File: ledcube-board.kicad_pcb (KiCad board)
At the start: 4 copper layers, 181 parts, among them J1 Conn_01x02, J10 molex_53261-0871, J11 1140084168, J12 molex_53261-0871, J2 molex_53261-0871, J3 molex_53261-0871, J4 molex_53261-0871, J5 molex_53261-0871, J6 molex_53261-0871, J7 molex_53261-0871, J8 molex_53261-0871, J9 molex_53261-0871, Q1 Q_NMOS_GDSD, Q2 Q_NMOS_GDSD, Q3 Q_NMOS_GDSD, Q4 Q_NMOS_GDSD, Q5 Q_NMOS_GDSD, Q6 Q_NMOS_GDSD, Q7 Q_NMOS_GDSD, Q8 Q_NMOS_GDSD, U1 LM1085IS-12, U10 ESP32-DEVKITC-32D, U11 IP4220CZ6, U12 IP4220CZ6, U13 XC9572XL-VQ64, U14 SN74LVCC3245APWR, U15 SN74LVCC3245APWR, U2 STP08CP05MTR, U3 STP08CP05MTR, U4 STP08CP05MTR, U5 STP08CP05MTR, U6 STP08CP05MTR, U7 STP08CP05MTR, U8 STP08CP05MTR, U9 STP08CP05MTR, X1 ASE-40MHz, X2 ASE-25MHz

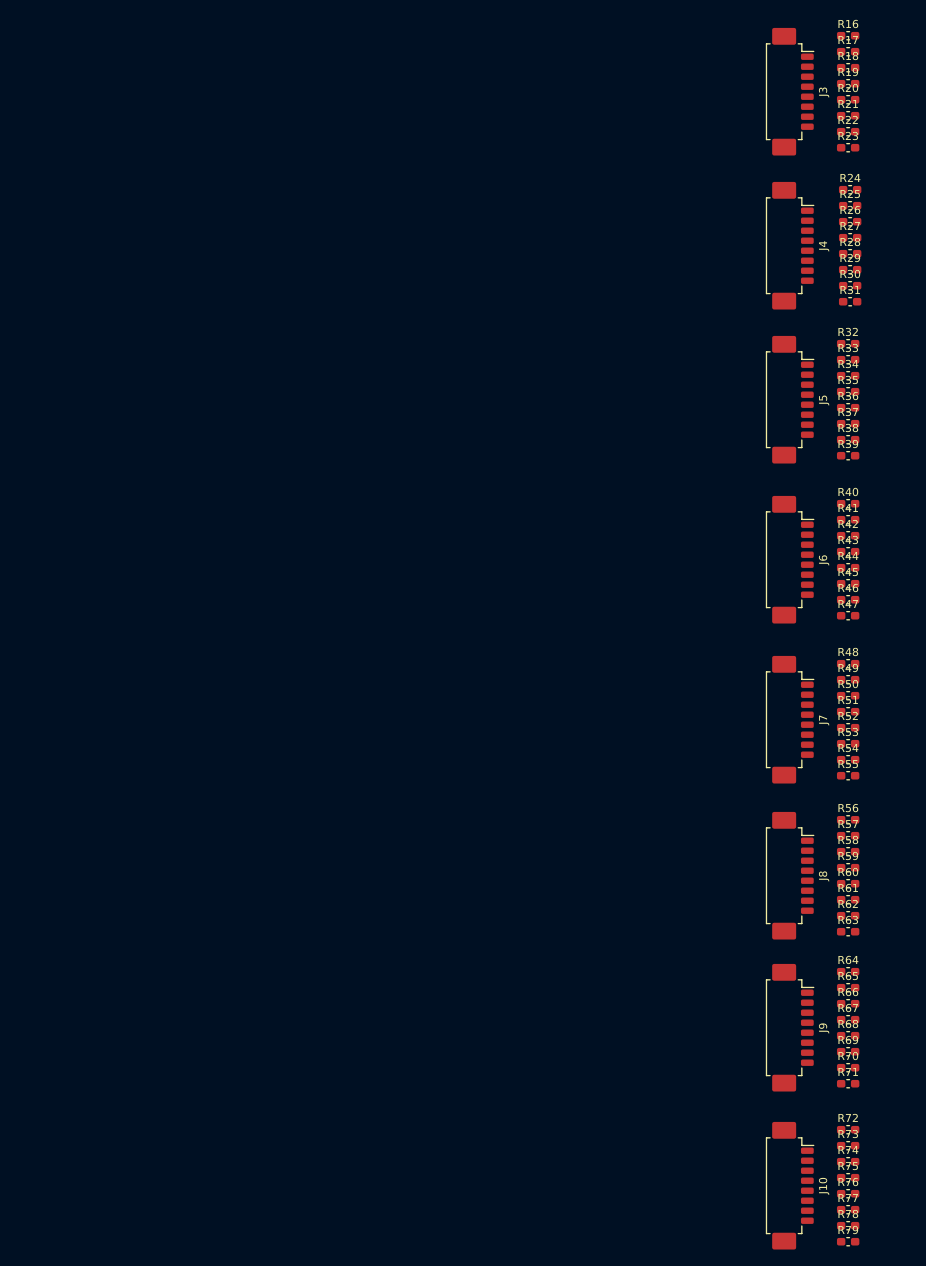
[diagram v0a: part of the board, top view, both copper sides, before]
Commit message: PCB: routing for connectors J3...J10
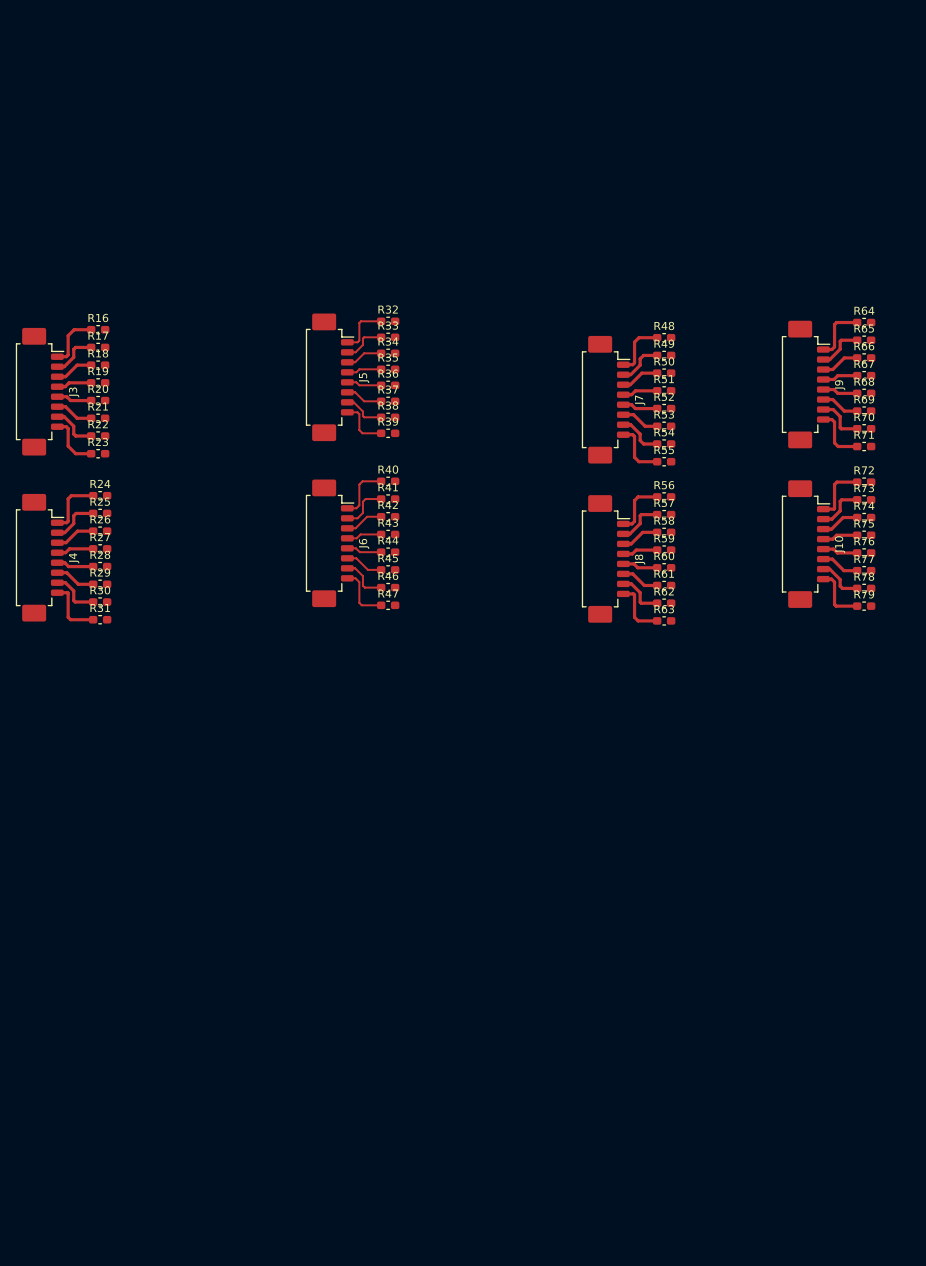
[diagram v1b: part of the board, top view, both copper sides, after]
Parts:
- moved R31 101.8 mm to (123.0, 88.5)
- moved R30 101.7 mm to (123.0, 86.3)
- moved R29 101.7 mm to (123.0, 84.1)
- moved R28 101.6 mm to (123.0, 81.9)
- moved J4 101.5 mm to (115.2, 80.8)
- moved R27 101.5 mm to (123.0, 79.6)
- moved R26 101.4 mm to (123.0, 77.4)
- moved R25 101.3 mm to (123.0, 75.2)
- moved R23 101.3 mm to (122.8, 67.8)
- moved R24 101.3 mm to (123.0, 73.0)
- moved R22 101.2 mm to (122.8, 65.5)
- moved R21 101.1 mm to (122.8, 63.3)
- moved R20 101.0 mm to (122.8, 61.1)
- moved J3 101.0 mm to (115.2, 60.0)
- moved R19 100.9 mm to (122.8, 58.9)
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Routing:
- net Net-(J4-Pad8): track 0.00 -> 7.63 mm
- net Net-(J4-Pad1): track 0.00 -> 7.51 mm
- net Net-(J10-Pad1): track 0.00 -> 7.38 mm
- net Net-(J8-Pad8): track 0.00 -> 7.26 mm
- net Net-(J10-Pad8): track 0.00 -> 7.26 mm
- net Net-(J9-Pad1): track 0.00 -> 7.26 mm
- net Net-(J6-Pad8): track 0.00 -> 7.15 mm
- net Net-(J8-Pad1): track 0.00 -> 7.15 mm
- net Net-(J7-Pad8): track 0.00 -> 7.15 mm
- net Net-(J6-Pad1): track 0.00 -> 7.15 mm
- net Net-(J7-Pad1): track 0.00 -> 7.15 mm
- net Net-(J9-Pad8): track 0.00 -> 7.15 mm
- net Net-(J3-Pad1): track 0.00 -> 7.03 mm
- net Net-(J3-Pad8): track 0.00 -> 6.91 mm
- net Net-(J5-Pad1): track 0.00 -> 6.60 mm
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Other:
- net class led_pwr added: clearance 0.3, trace_width 0.4, via_dia 1, via_drill 0.5

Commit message: Complete routing of single part of led connectors
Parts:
- moved U6 392.7 mm to (-48.2, 73.0)
- moved U7 382.1 mm to (-49.2, 95.2)
- moved C12 370.9 mm to (-47.4, 87.6), turned to 180 degrees
- moved C11 361.4 mm to (-46.4, 65.5), turned to 180 degrees
- moved C14 354.7 mm to (-14.2, 59.8), turned to 180 degrees
- moved U9 348.7 mm to (-16.0, 67.3)
- moved U8 347.6 mm to (14.0, 74.1)
- moved C13 319.5 mm to (15.8, 66.6), turned to 180 degrees
- moved C8 302.1 mm to (62.6, 57.5), turned to 180 degrees
- moved U3 283.9 mm to (60.8, 65.0)
- moved C9 282.2 mm to (70.4, 77.4), turned to 270 degrees
- moved U2 279.1 mm to (60.8, 44.2)
- moved C7 278.9 mm to (62.6, 36.7), turned to 180 degrees
- moved U4 269.1 mm to (78.0, 79.2), turned to 90 degrees
- moved U5 255.5 mm to (98.7, 79.2), turned to 90 degrees
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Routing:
- net Net-(R39-Pad2): track 0.00 -> 22.6 mm
- net Net-(R47-Pad2): track 0.00 -> 22.6 mm
- net Net-(R31-Pad2): track 0.00 -> 22.6 mm
- net Net-(R79-Pad2): track 0.00 -> 22.6 mm
- net Net-(R71-Pad2): track 0.00 -> 22.6 mm
- net Net-(R63-Pad2): track 0.00 -> 22.6 mm
- net Net-(R23-Pad2): track 0.00 -> 22.6 mm
- net Net-(R55-Pad2): track 0.00 -> 22.6 mm
- net Net-(R46-Pad2): track 0.00 -> 20.1 mm
- net Net-(R38-Pad2): track 0.00 -> 20.1 mm
- net Net-(R22-Pad2): track 0.00 -> 20.1 mm
- net Net-(R62-Pad2): track 0.00 -> 20.1 mm
- net Net-(R54-Pad2): track 0.00 -> 20.1 mm
- net Net-(R30-Pad2): track 0.00 -> 20.1 mm
- net Net-(R70-Pad2): track 0.00 -> 20.1 mm
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
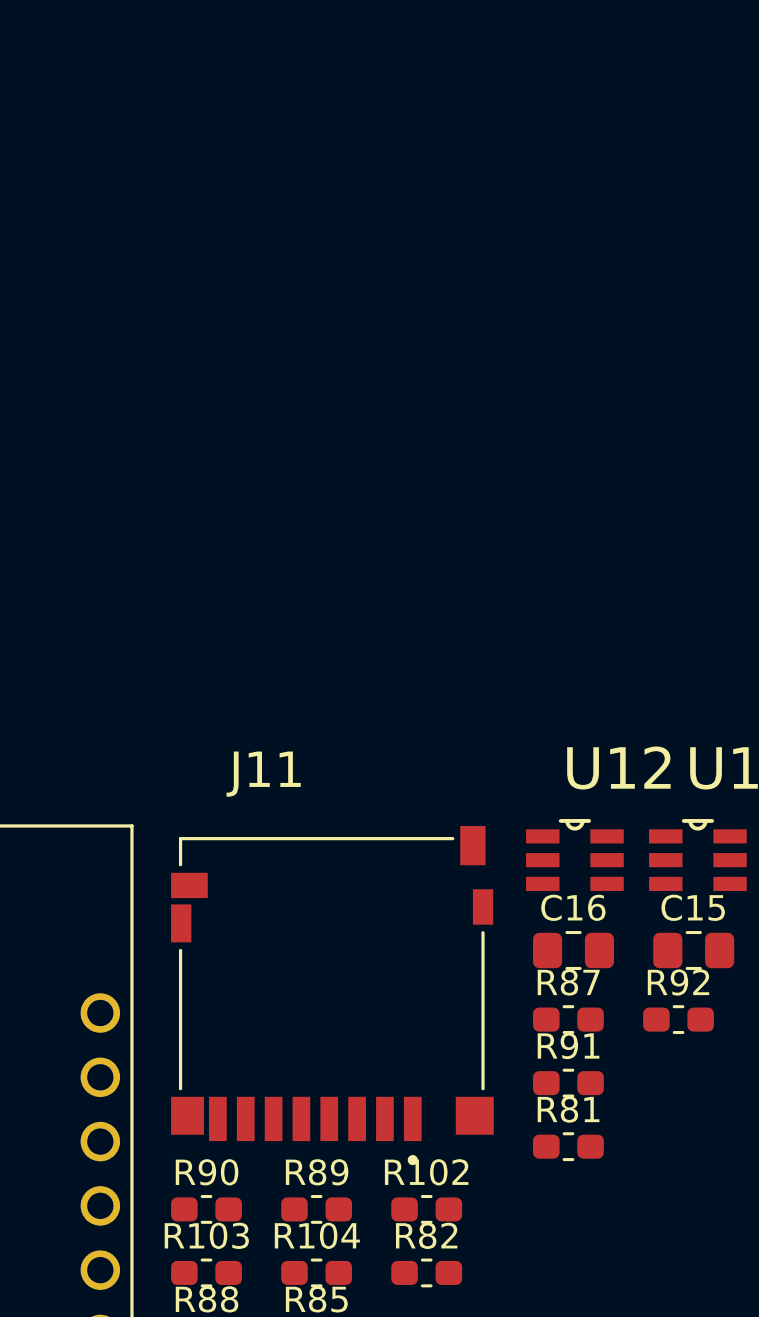
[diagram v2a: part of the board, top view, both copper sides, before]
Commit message: Schematic: Change uSD connector (now is a Molex one)
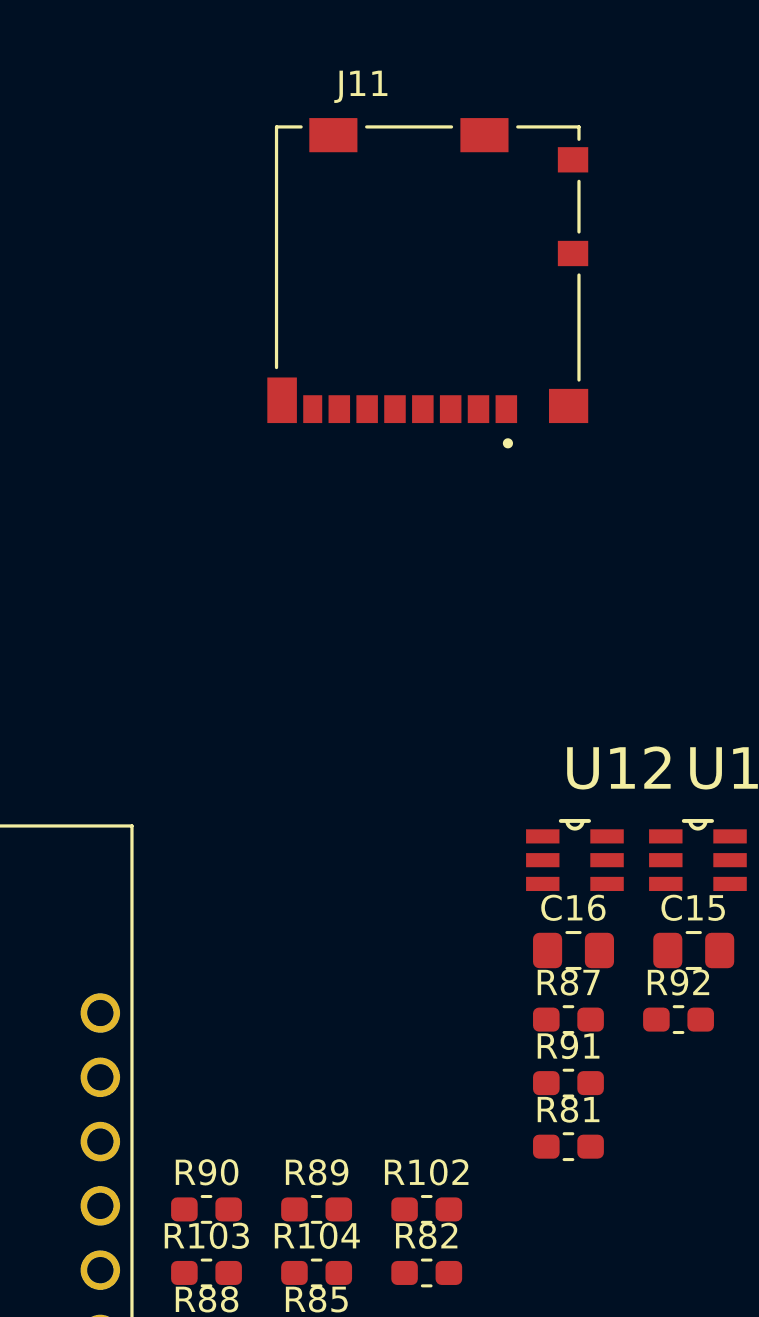
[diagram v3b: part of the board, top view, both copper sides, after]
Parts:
- J11: value 1140084168 -> 104031-0811; footprint AMPHENOL_1140084168 -> MOLEX_104031-0811
- moved J11 32.8 mm to (340.0, 42.8)
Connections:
- J8 pad MP: Net-(J8-PadMP) -> GND

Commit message: PCB: partial routing of CPLD part
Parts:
- moved J2 421.8 mm to (-9.00, 137.2), turned to 180 degrees
- moved H3 414.8 mm to (45.2, 28.8)
- moved H4 412.3 mm to (45.5, 95.5)
- moved R6 386.0 mm to (59.6, 150.0), turned to 90 degrees
- moved R5 383.7 mm to (59.0, 161.8), turned to 270 degrees
- moved Q4 382.6 mm to (53.1, 126.0), turned to 180 degrees
- moved Q1 377.6 mm to (52.6, 160.8), turned to 180 degrees
- moved R7 375.2 mm to (59.7, 138.0), turned to 90 degrees
- moved R8 374.4 mm to (59.9, 125.9), turned to 90 degrees
- moved Q3 365.2 mm to (52.9, 138.2), turned to 180 degrees
- moved R12 364.9 mm to (79.3, 125.6), turned to 90 degrees
- moved R11 364.7 mm to (79.4, 134.7), turned to 90 degrees
- moved R9 362.9 mm to (79.4, 154.5), turned to 90 degrees
- moved R10 356.6 mm to (79.7, 144.7), turned to 90 degrees
- moved Q6 356.2 mm to (71.7, 144.6), turned to 180 degrees
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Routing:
- net /pl.sch/~DATA_OE_3V3: track 0.00 -> 21.6 mm
- net /pl.sch/DATA_ROW1_3V3: track 0.00 -> 21.1 mm
- net /pl.sch/DATA_ROW2_3V3: track 0.00 -> 20.3 mm
- net /pl.sch/DATA_ROW3_3V3: track 0.00 -> 19.3 mm
- net /pl.sch/DATA_ROW7_3V3: track 0.00 -> 19.2 mm
- net /pl.sch/DATA_ROW4_3V3: track 0.00 -> 18.8 mm
- net /pl.sch/DATA_ROW5_3V3: track 0.00 -> 17.7 mm
- net /pl.sch/DATA_ROW8_3V3: track 0.00 -> 17.4 mm
- net /pl.sch/DATA_ROW6_3V3: track 0.00 -> 16.5 mm
- net /pl.sch/DATA_CLK_3V3: track 0.00 -> 14.9 mm
- net /pl.sch/DATA_LE_3V3: track 0.00 -> 14.1 mm
- net /pl.sch/TDI: track 0.00 -> 10.9 mm
- net /pl.sch/TMS: track 0.00 -> 10.7 mm
- net /pl.sch/TCK: track 0.00 -> 10.6 mm
- net /pl.sch/TDO: track 0.00 -> 9.99 mm
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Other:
- net class layer_selection added: clearance 0.3, trace_width 0.6, via_dia 1.2, via_drill 0.6
- net class led_pwr: via_dia 1 -> 0.8; via_drill 0.5 -> 0.4

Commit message: PCB: Placement of all top layer
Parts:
- moved R80 154.8 mm to (109.5, 151.5), turned to 90 degrees
- moved R104 133.0 mm to (99.0, 151.5), turned to 90 degrees
- moved R102 132.7 mm to (106.0, 151.5), turned to 90 degrees
- moved J2 131.1 mm to (115.8, 97.0), turned to 0 degrees
- moved R103 127.2 mm to (102.5, 151.5), turned to 90 degrees
- moved J11 112.9 mm to (194.2, 36.8), turned to 0 degrees
- moved R6 96.7 mm to (100.6, 62.5), turned to 180 degrees
- moved R5 93.6 mm to (100.6, 78.0), turned to 180 degrees
- moved Q2 92.6 mm to (100.6, 69.9), turned to 270 degrees
- moved R10 91.4 mm to (119.4, 62.3), turned to 180 degrees
- moved Q1 89.4 mm to (100.6, 85.4), turned to 270 degrees
- moved Q6 88.4 mm to (119.3, 70.1), turned to 270 degrees
- moved R9 86.4 mm to (119.5, 78.0), turned to 180 degrees
- moved Q5 83.5 mm to (119.3, 85.4), turned to 270 degrees
- moved R8 80.7 mm to (109.9, 62.5), turned to 180 degrees
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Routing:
- net /layer_selector.sch/LAYER_SEL8: track 6.30 -> 44.9 mm
- net /layer_selector.sch/LAYER_SEL2: track 6.30 -> 42.1 mm
- net /layer_selector.sch/LAYER_SEL6: track 6.30 -> 39.6 mm
- net /layer_selector.sch/LAYER_SEL4: track 6.30 -> 36.2 mm
- net /layer_selector.sch/LAYER_SEL1: track 6.30 -> 26.8 mm
- net /layer_selector.sch/LAYER_SEL7: track 6.30 -> 24.6 mm
- net /layer_selector.sch/LAYER_SEL5: track 6.30 -> 19.7 mm
- net /layer_selector.sch/LAYER_SEL3: track 6.30 -> 19.3 mm
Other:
- net class layer_selection: trace_width 0.6 -> 0.8; via_drill 0.6 -> 0.8
